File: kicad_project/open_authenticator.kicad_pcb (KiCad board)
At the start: 2 copper layers, 82 x 42 mm, 86 parts, among them IC1 TPS22919DCKR, J1 Conn_01x02_Female, J2 TYPE-C-31-M-17, J3 S2B-PH-SM4-TB(LF)(SN), P1 SSD1306_ribbon, Q1 DMP2305U-7, SW1 UP, SW2 DOWN, SW3 BOOT/SELECT, SW4 RESET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

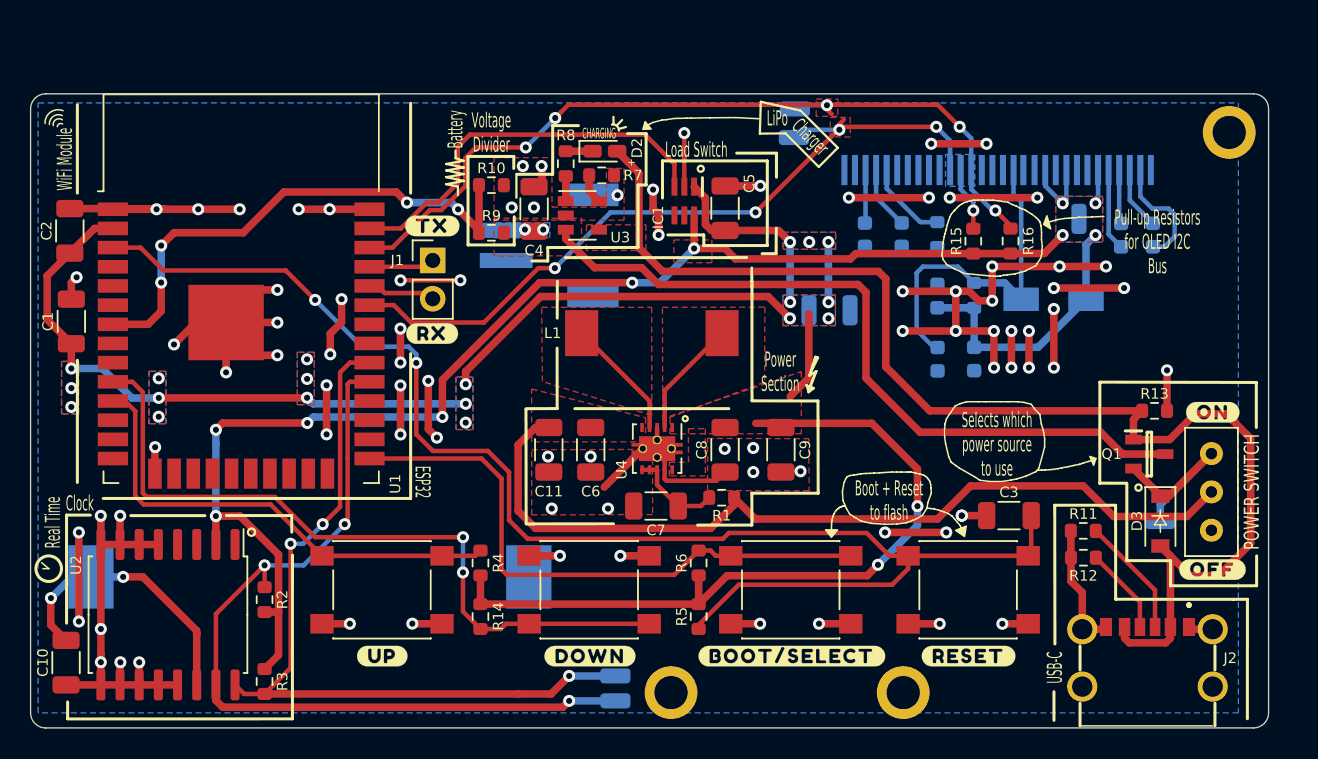
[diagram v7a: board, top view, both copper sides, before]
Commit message: Updated silkscreen to include bounds of the OLED
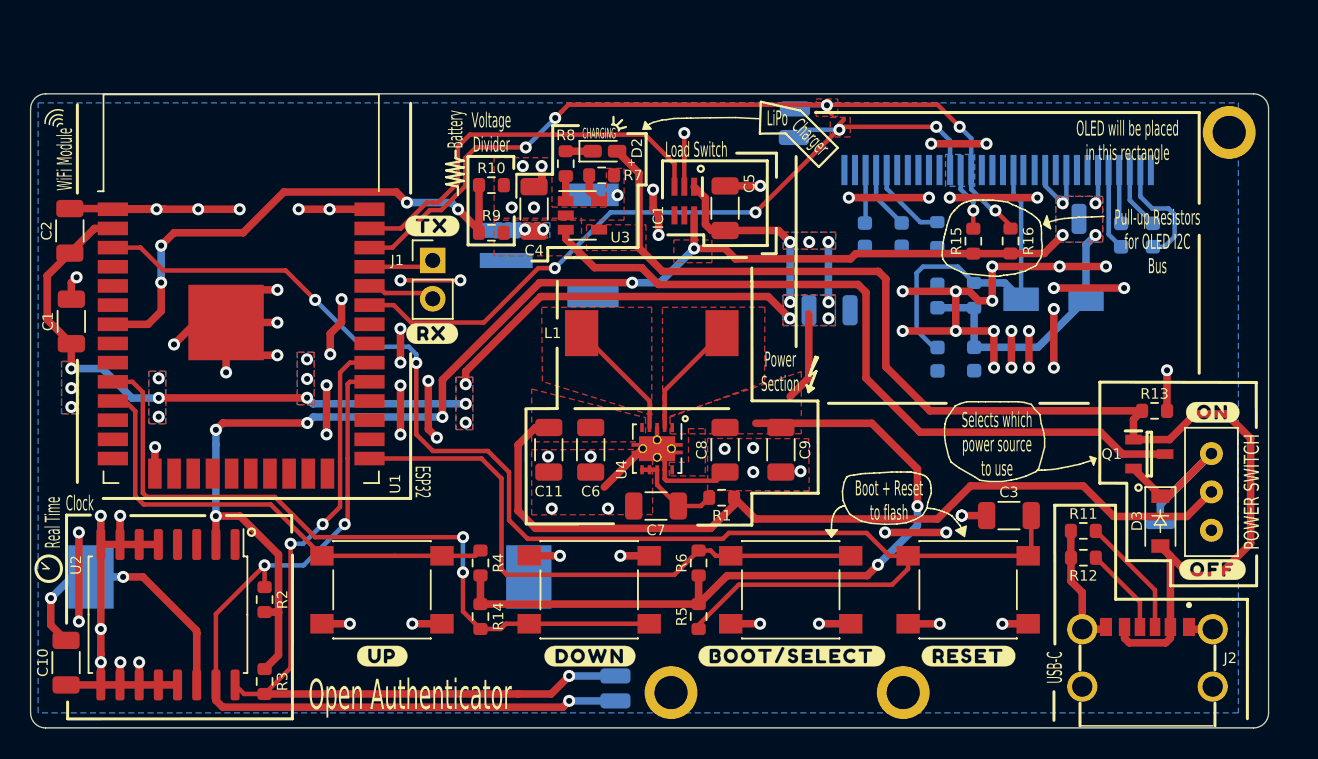
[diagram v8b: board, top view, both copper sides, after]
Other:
- board text added: "OLED will be placed in this rectangle"
- board text added: "Open Authenticator"
